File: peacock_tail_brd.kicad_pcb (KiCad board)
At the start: 2 copper layers, 90.8 x 36.1 mm, 27 parts, among them J1 Conn_01x03, J10 Screw_Terminal_01x02, J2 Conn_01x03, J3 Conn_01x03, J4 Conn_01x03, J5 Conn_01x03, J7 Conn_01x04, J8 Conn_01x04, U1 RP2040-ZERO, U2 L7805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

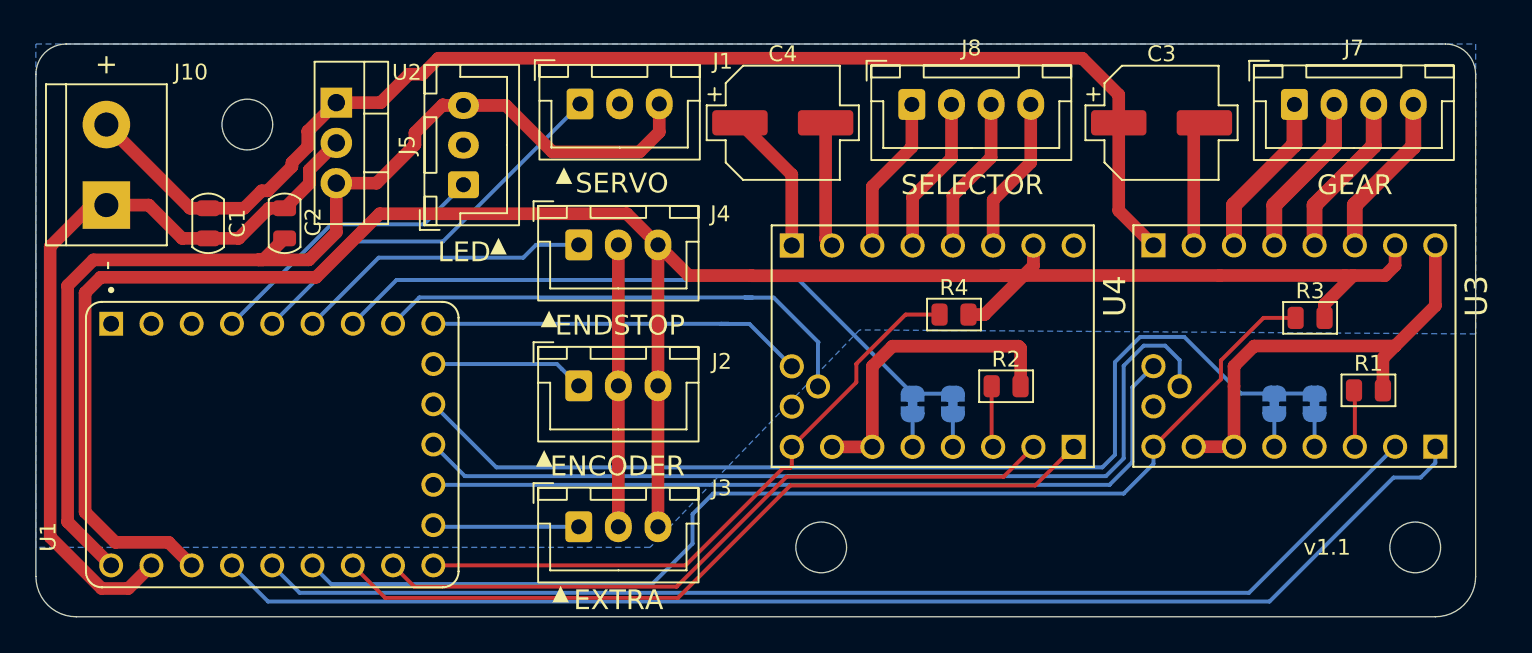
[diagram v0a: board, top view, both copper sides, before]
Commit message: 3d model alignment
Signed-off-by: Sezgin AÇIKGÖZ <sacikgoz@tarla-fel.org>
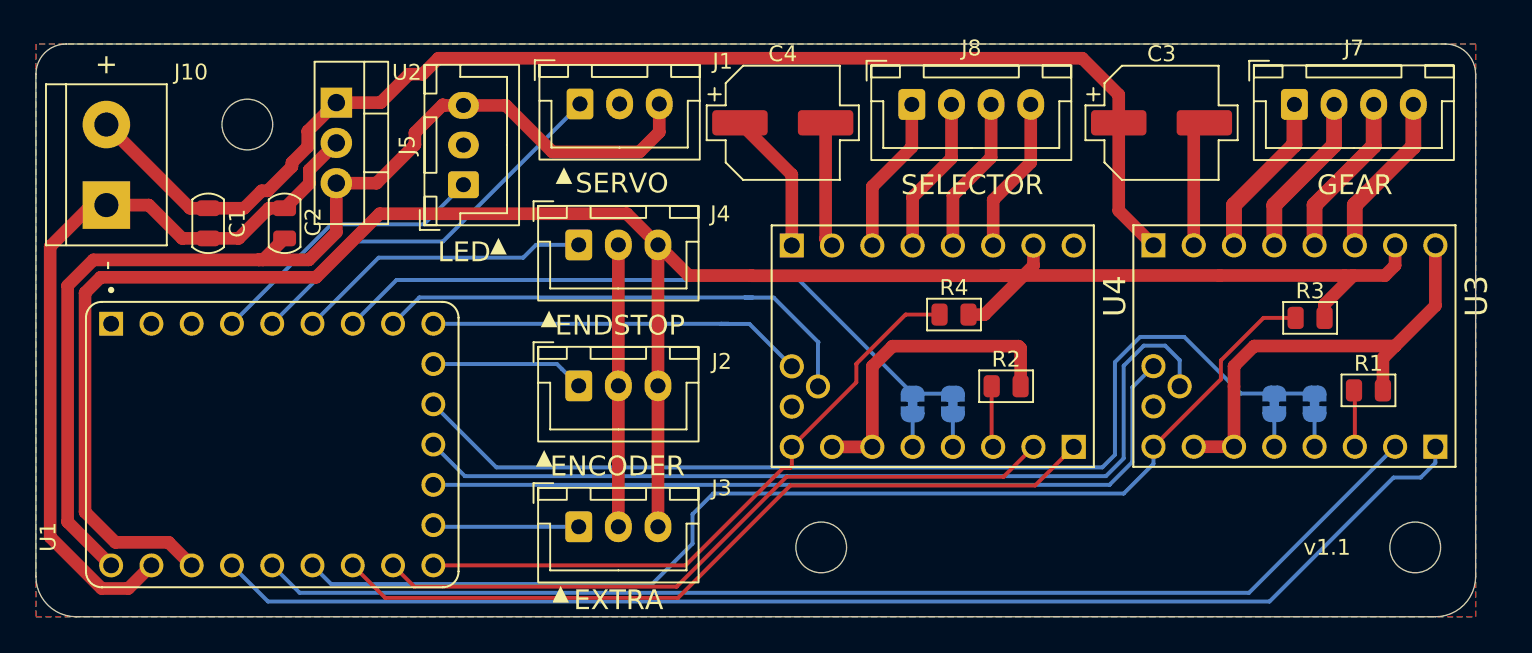
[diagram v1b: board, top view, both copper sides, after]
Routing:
- added copper zone on F.Cu, net GND
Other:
- board text added: "GP3"
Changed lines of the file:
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@@
 			(at 0 4.2 0)
 			(layer "F.Fab")
+			(hide yes)
 			(effects
 				(font
@@
 		(tags "terminal block bornier2")
 		(property "Reference" "J10"
-			(at -3.302 -5.334 180)
+			(at -3.302 -5.334 0)
 			(layer "F.SilkS")
 			(effects
@@
 			(at 2.54 5.08 90)
 			(layer "F.Fab")
+			(hide yes)
 			(effects
 				(font
@@
 		)
 		(property "Datasheet" "~"
-			(at 0 0 270)
+			(at 0 0 90)
 			(layer "F.Fab")
 			(hide yes)
@@
 		)
 		(property "Description" ""
-			(at 0 0 270)
+			(at 0 0 90)
 			(layer "F.Fab")
 			(hide yes)
@@
 			(at 0 4.2 0)
 			(layer "F.Fab")
+			(hide yes)
 			(effects
 				(font
@@
 			(at 0 4.2 0)
 			(layer "F.Fab")
+			(hide yes)
 			(effects
 				(font
@@
 			(at 19.07 11.411 90)
 			(layer "F.Fab")
+			(hide yes)
 			(effects
 				(font
@@
 		(model "${KIPRJMOD}/peacock_tail_brd.pretty/packages3d/BTT TMC2209-V1.2.STEP"
 			(offset
-				(xyz 0 0 9.4)
+				(xyz 0 0 10.9)
 			)
 			(scale
@@
 			)
 			(rotate
-				(xyz -90 0 180)
+				(xyz -90 -0 180)
 			)
 		)
@@
 			(at 19.07 11.411 90)
 			(layer "F.Fab")
+			(hide yes)
 			(effects
 				(font
@@
 		(model "${KIPRJMOD}/peacock_tail_brd.pretty/packages3d/BTT TMC2209-V1.2.STEP"
 			(offset
-				(xyz 0 0 9.4)
+				(xyz 0 0 10.9)
 			)
 			(scale
@@
 			)
 			(rotate
-				(xyz -90 0 180)
+				(xyz -90 -0 180)
 			)
 		)
@@
 		)
 	)
+	(gr_text "+5V"
+		(at 131.26 92.69 0)
+		(layer "B.SilkS")
+		(effects
+			(font
+				(size 1 1)
+				(thickness 0.15)
+			)
+			(justify mirror)
+		)
+	)
+	(gr_text "GND"
+		(at 131.26 95.23 0)
+		(layer "B.SilkS")
+		(effects
+			(font
+				(size 1 1)
+				(thickness 0.15)
+			)
+			(justify mirror)
+		)
+	)
+	(gr_text "GP3"
+		(at 131.26 97.81 0)
+		(layer "B.SilkS")
+		(effects
+			(font
+				(size 1 1)
+				(thickness 0.15)
+			)
+			(justify mirror)
+		)
+	)
 	(gr_text "UART"
 		(at 158.18 109.145 0)
@@
 		)
 	)
+	(point
+		(at 101.615 88.815)
+		(size 1)
+		(layer "F.Cu")
+	)
+	(point
+		(at 101.615 124.94)
+		(size 1)
+		(layer "F.Cu")
+	)
+	(point
+		(at 192.42 88.815)
+		(size 1)
+		(layer "F.Cu")
+	)
+	(point
+		(at 192.42 124.94)
+		(size 1)
+		(layer "F.Cu")
+	)
 	(segment
 		(start 177.18 110.405)
@@
 	(zone
 		(net "GND")
-		(layer "B.Cu")
-		(hatch edge 0.508)
+		(layers "F.Cu" "B.Cu")
+		(hatch edge 0.5)
 		(connect_pads
 			(clearance 0.508)
 		)
-		(min_thickness 0.254)
-		(fill
-			(thermal_gap 0.508)
-			(thermal_bridge_width 0.508)
+		(min_thickness 0.25)
+		(fill yes
+			(thermal_gap 0.5)
+			(thermal_bridge_width 0.5)
 			(island_removal_mode 0)
 		)
 		(polygon
 			(pts
-				(xy 192.42 107.103) (xy 153.558 106.849) (xy 140.35 120.565) (xy 101.615 120.565) (xy 101.615 88.815)
-				(xy 192.42 88.815)
+				(xy 101.615 124.94) (xy 192.42 124.94) (xy 192.42 88.815) (xy 101.615 88.815)
 			)
 		)

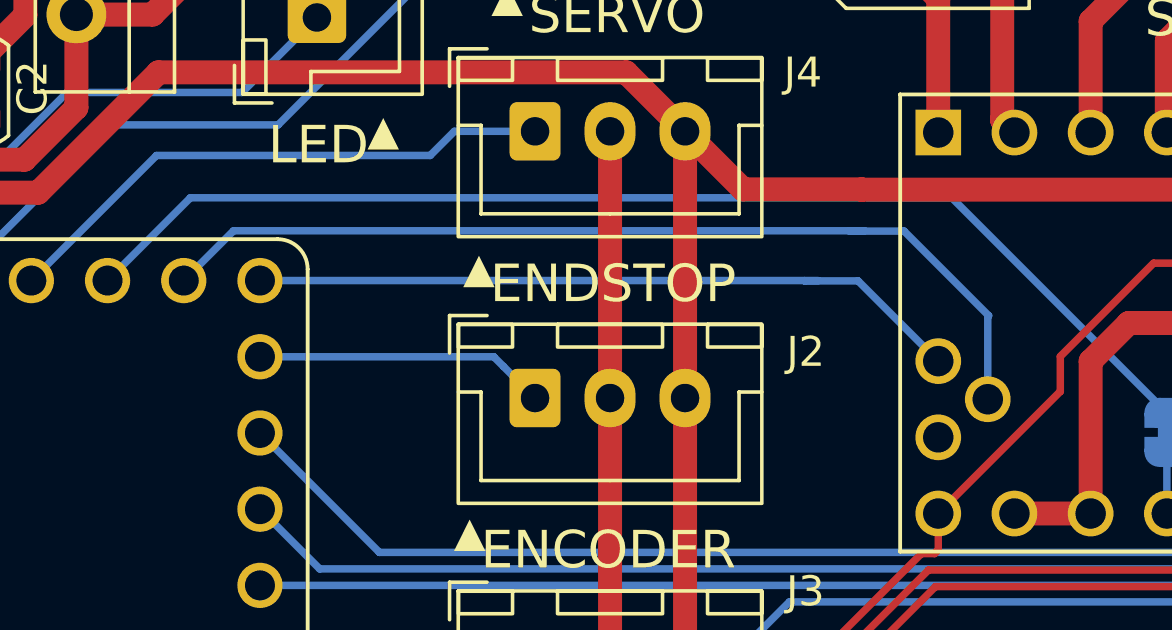
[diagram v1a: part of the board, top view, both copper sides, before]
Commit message: connected missing nets
Signed-off-by: Sezgin AÇIKGÖZ <sacikgoz@tarla-fel.org>
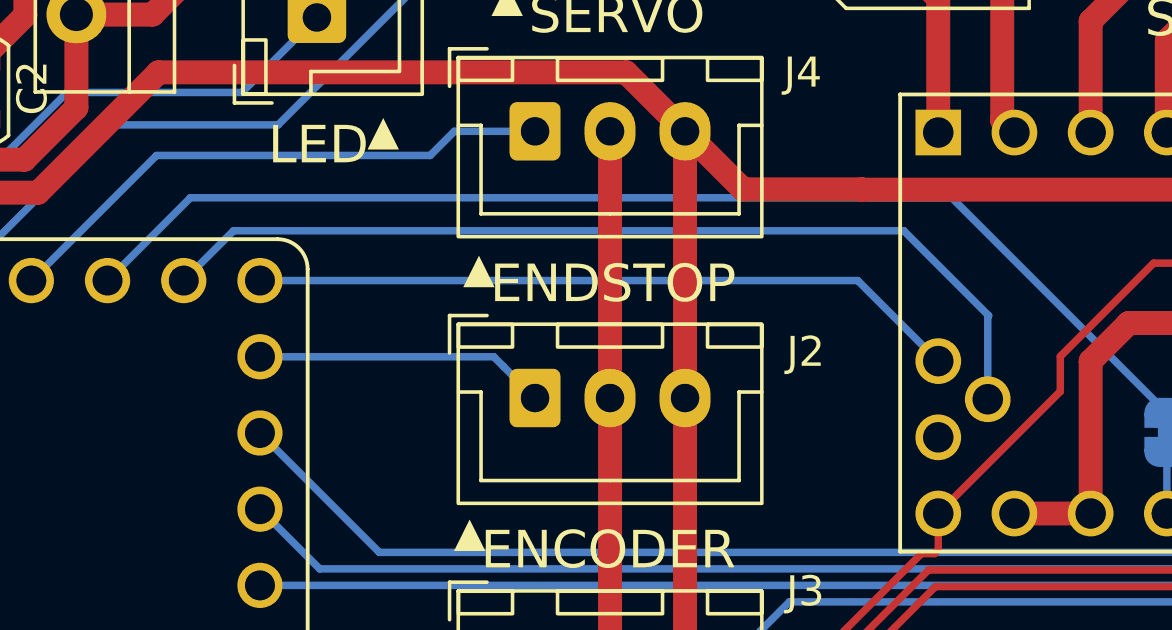
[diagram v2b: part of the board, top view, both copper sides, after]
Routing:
- net S-DIAG: track 32.0 -> 31.5 mm
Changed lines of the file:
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@@
 	)
 	(segment
-		(start 148.15 104.81)
+		(start 148.14 104.8)
+		(end 125.8 104.8)
+		(width 0.25)
+		(layer "B.Cu")
+		(net "S-DIAG")
+	)
+	(segment
+		(start 150.97 107.63)
+		(end 148.14 104.8)
+		(width 0.25)
+		(layer "B.Cu")
+		(net "S-DIAG")
+	)
+	(segment
+		(start 150.941 110.415)
+		(end 150.941 107.659)
+		(width 0.25)
+		(layer "B.Cu")
+		(net "S-DIAG")
+	)
+	(segment
+		(start 125.8 104.8)
+		(end 124.14 106.46)
+		(width 0.25)
+		(layer "B.Cu")
+		(net "S-DIAG")
+	)
+	(segment
+		(start 150.941 107.659)
 		(end 150.97 107.63)
 		(width 0.25)
@@
 	)
 	(segment
-		(start 146.33 104.8)
-		(end 146.83 104.8)
-		(width 0.25)
-		(layer "B.Cu")
-		(net "S-DIAG")
-	)
-	(segment
-		(start 150.941 107.659)
-		(end 150.941 110.415)
-		(width 0.25)
-		(layer "B.Cu")
-		(net "S-DIAG")
-	)
-	(segment
-		(start 125.8 104.8)
-		(end 146.33 104.8)
-		(width 0.25)
-		(layer "B.Cu")
-		(net "S-DIAG")
-	)
-	(segment
-		(start 146.34 104.81)
-		(end 146.33 104.8)
-		(width 0.25)
-		(layer "B.Cu")
-		(net "S-DIAG")
-	)
-	(segment
-		(start 124.14 106.46)
-		(end 125.8 104.8)
-		(width 0.25)
-		(layer "B.Cu")
-		(net "S-DIAG")
-	)
-	(segment
-		(start 148.15 104.81)
-		(end 146.34 104.81)
-		(width 0.25)
-		(layer "B.Cu")
-		(net "S-DIAG")
-	)
-	(segment
-		(start 150.97 107.63)
-		(end 150.941 107.659)
-		(width 0.25)
-		(layer "B.Cu")
-		(net "S-DIAG")
-	)
-	(segment
-		(start 144.84 106.47)
-		(end 144.83 106.46)
+		(start 146.615 106.47)
+		(end 146.605 106.46)
 		(width 0.25)
 		(layer "B.Cu")
@@
 	)
 	(segment
-		(start 146.615 106.47)
-		(end 144.84 106.47)
-		(width 0.25)
-		(layer "B.Cu")
-		(net "S-INDEX")
-	)
-	(segment
-		(start 144.83 106.46)
+		(start 146.605 106.46)
 		(end 126.68 106.46)
 		(width 0.25)
 		(layer "B.Cu")
-		(net "S-INDEX")
-	)
-	(segment
-		(start 145.295 106.46)
-		(end 144.83 106.46)
-		(width 0.25)
-		(layer "B.Cu")

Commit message: lm2596 update
Signed-off-by: Sezgin AÇIKGÖZ <sacikgoz@tarla-fel.org>
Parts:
- added C5: 220uF/10V, PCM_Capacitor_SMD_AKL:CP_Elec_6.3x7.7, F.Cu at (121.5, 95.0)
- added C6: 100nF, Capacitor_SMD:C_0603_1608Metric, F.Cu at (82.2, 98.7)
- added D1: SS34, Diode_SMD:D_SMA, F.Cu at (130.7, 107.2)
- added D2: LED, LED_SMD:LED_0603_1608Metric, F.Cu at (79.7, 106.6)
- added L1: 47uH, Inductor_SMD:L_Bourns_SRR1208_12.7x12.7mm, B.Cu at (117.9, 97.0)
- added R5: 1K, Resistor_SMD:R_0603_1608Metric, F.Cu at (82.2, 101.2)
- added R6: 4K7, Resistor_SMD:R_0603_1608Metric, F.Cu at (82.2, 103.8)
- added RV1: 10K, Potentiometer_THT:Potentiometer_Bourns_3296W_Vertical, F.Cu at (120.5, 102.4)
- C1: value 0.33uF/50V -> 100uF; footprint PCM_Capacitor_SMD_AKL:C_0805_2012Metric -> PCM_Capacitor_SMD_AKL:CP_Elec_6.3x7.7
- C2: value 0.1uF/50V -> 100nF; footprint PCM_Capacitor_SMD_AKL:C_0805_2012Metric -> Capacitor_SMD:C_0603_1608Metric
- U2: value L7805 -> LM2596S-ADJ; footprint Package_TO_SOT_THT:TO-220-3_Vertical -> Package_TO_SOT_SMD:TO-263-5_TabPin3; moved to B.Cu
- moved H2 143.5 mm to (3.48, 3.48)
- moved C2 34.7 mm to (82.9, 95.9), turned to 0 degrees
- moved U2 21.4 mm to (117.8, 113.7), turned to 0 degrees
- moved C1 5.37 mm to (114.0, 95.0)
- renumbered J10 to J6
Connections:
- C1 pad 1: VDC -> VIN
- C2 pad 1: +5V -> VIN
- C3 pad 1: VDC -> VIN
- C4 pad 1: VDC -> VIN
- J6 pad 2: VDC -> VIN
- U2 pad 1: VDC -> VIN
- U2 pad 2: GND -> /SW
- U2 pad 3: +5V -> GND
- U3 pad JP2_1: VDC -> VIN
- U4 pad JP2_1: VDC -> VIN
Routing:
- net VIN: track 0.00 -> 117.9 mm
- net VDC: track 91.1 -> 0.00 mm
- net +5V: track 68.8 -> 72.4 mm
- net LED: track 18.2 -> 21.7 mm
- net SERVO: track 26.0 -> 28.8 mm
- net GND: track 132.3 -> 133.4 mm
